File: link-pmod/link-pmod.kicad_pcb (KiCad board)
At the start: 2 copper layers, 31.8 x 25.4 mm, 3 parts, among them J1 Mini-DIN-8, J2 PMOD, J3 GB

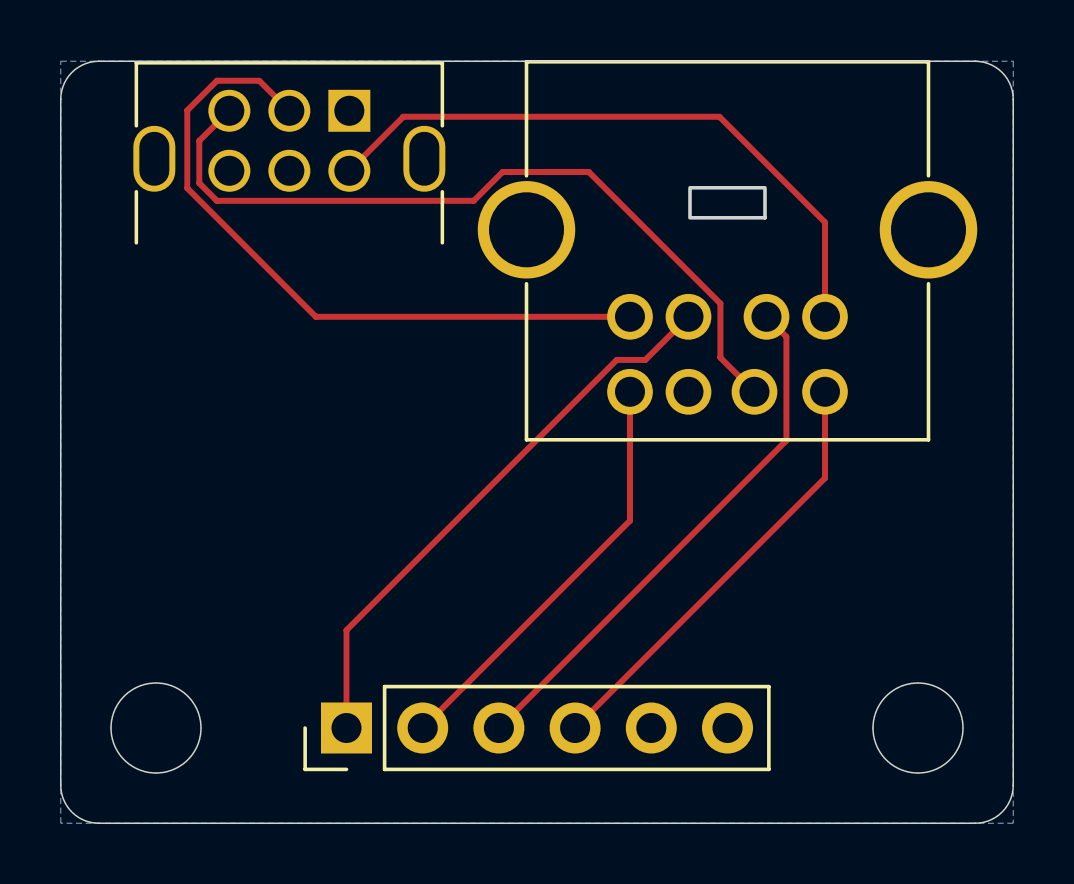
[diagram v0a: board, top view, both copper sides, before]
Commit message: Use M3 mounting screw footprint
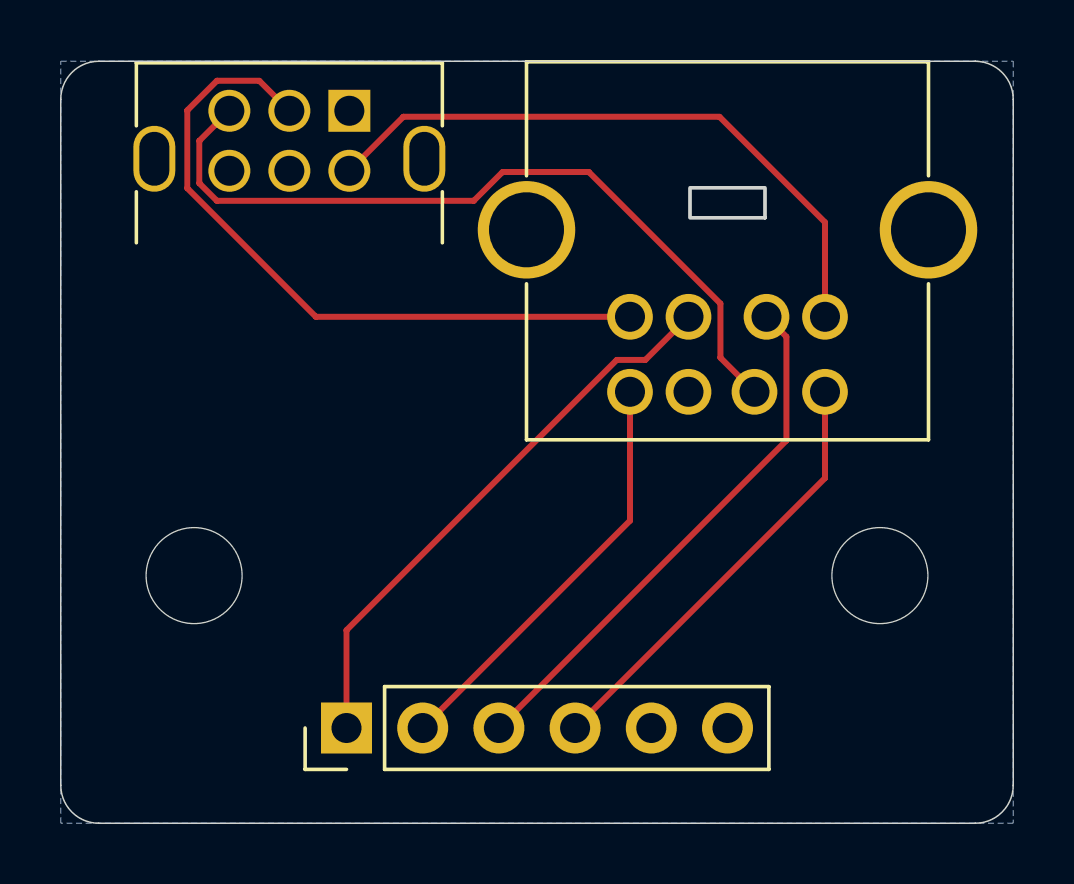
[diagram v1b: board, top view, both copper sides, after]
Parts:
- added REF**: MountingHole_3.2mm_M3, MountingHole:MountingHole_3.2mm_M3, B.Cu at (93.3, 125.1)
- added REF**: MountingHole_3.2mm_M3, MountingHole:MountingHole_3.2mm_M3, B.Cu at (116.2, 125.1)
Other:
- outline, holes or cut-outs redrawn
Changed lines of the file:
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@@
 		)
+	)
+	(footprint "MountingHole:MountingHole_3.2mm_M3"
+		(layer "B.Cu")
+		(at 93.345 125.095 180)
+		(descr "Mounting Hole 3.2mm, M3, no annular, generated by kicad-footprint-generator mountinghole.py")
+		(tags "mountinghole M3")
+		(property "Reference" "REF**"
+			(at 0 4.15 0)
+			(layer "B.SilkS")
+			(hide yes)
+			(effects
+				(font
+					(size 1 1)
+					(thickness 0.15)
+				)
+				(justify mirror)
+			)
+		)
+		(property "Value" "MountingHole_3.2mm_M3"
+			(at 0 -4.15 0)
+			(layer "B.Fab")
+			(hide yes)
+			(effects
+				(font
+					(size 1 1)
+					(thickness 0.15)
+				)
+				(justify mirror)
+			)
+		)
+		(property "Datasheet" ""
+			(at 0 0 0)
+			(layer "B.Fab")
+			(hide yes)
+			(effects
+				(font
+					(size 1.27 1.27)
+					(thickness 0.15)
+				)
+				(justify mirror)
+			)
+		)
+		(property "Description" ""
+			(at 0 0 0)
+			(layer "B.Fab")
+			(hide yes)
+			(effects
+				(font
+					(size 1.27 1.27)
+					(thickness 0.15)
+				)
+				(justify mirror)
+			)
+		)
+		(attr board_only exclude_from_pos_files exclude_from_bom)
+		(fp_circle
+			(center 0 0)
+			(end 3.2 0)
+			(stroke
+				(width 0.15)
+				(type solid)
+			)
+			(fill no)
+			(layer "Cmts.User")
+		)
+		(fp_circle
+			(center 0 0)
+			(end 3.45 0)
+			(stroke
+				(width 0.05)
+				(type solid)
+			)
+			(fill no)
+			(layer "B.CrtYd")
+		)
+		(pad "" np_thru_hole circle
+			(at 0 0 180)
+			(size 3.2 3.2)
+			(drill 3.2)
+			(layers "*.Cu" "*.Mask")
+		)
+		(embedded_fonts no)
+	)
+	(footprint "MountingHole:MountingHole_3.2mm_M3"
+		(layer "B.Cu")
+		(at 116.205 125.095 180)
+		(descr "Mounting Hole 3.2mm, M3, no annular, generated by kicad-footprint-generator mountinghole.py")
+		(tags "mountinghole M3")
+		(property "Reference" "REF**"
+			(at 0 4.15 0)
+			(layer "B.SilkS")
+			(hide yes)
+			(effects
+				(font
+					(size 1 1)
+					(thickness 0.15)
+				)
+				(justify mirror)
+			)
+		)
+		(property "Value" "MountingHole_3.2mm_M3"
+			(at 0 -4.15 0)
+			(layer "B.Fab")
+			(hide yes)
+			(effects
+				(font
+					(size 1 1)
+					(thickness 0.15)
+				)
+				(justify mirror)
+			)
+		)
+		(property "Datasheet" ""
+			(at 0 0 0)
+			(layer "B.Fab")
+			(hide yes)
+			(effects
+				(font
+					(size 1.27 1.27)
+					(thickness 0.15)
+				)
+				(justify mirror)
+			)
+		)
+		(property "Description" ""
+			(at 0 0 0)
+			(layer "B.Fab")
+			(hide yes)
+			(effects
+				(font
+					(size 1.27 1.27)
+					(thickness 0.15)
+				)
+				(justify mirror)
+			)
+		)
+		(attr board_only exclude_from_pos_files exclude_from_bom)
+		(fp_circle
+			(center 0 0)
+			(end 3.2 0)
+			(stroke
+				(width 0.15)
+				(type solid)
+			)
+			(fill no)
+			(layer "Cmts.User")
+		)
+		(fp_circle
+			(center 0 0)
+			(end 3.45 0)
+			(stroke
+				(width 0.05)
+				(type solid)
+			)
+			(fill no)
+			(layer "B.CrtYd")
+		)
+		(pad "" np_thru_hole circle
+			(at 0 0 180)
+			(size 3.2 3.2)
+			(drill 3.2)
+			(layers "*.Cu" "*.Mask")
+		)
+		(embedded_fonts no)
 	)
 	(gr_line
@@
 		(layer "Edge.Cuts")
 	)
-	(gr_circle
-		(center 117.475 130.175)
-		(end 118.975 130.175)
-		(stroke
-			(width 0.05)
-			(type solid)
-		)
-		(fill no)
-		(layer "Edge.Cuts")
-	)
 	(gr_line
 		(start 88.899998 132.080001)
@@
 		(layer "Edge.Cuts")
 	)
-	(gr_circle
-		(center 92.075 130.175)
-		(end 93.575 130.175)
-		(stroke
-			(width 0.05)
-			(type solid)
-		)
-		(fill no)
-		(layer "Edge.Cuts")
-	)
